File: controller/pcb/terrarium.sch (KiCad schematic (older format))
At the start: 53 parts, among them K1 G3MB-202P, K2 G3MB-202P, K3 G3MB-202P, Q1 S8050, Q2 S8050, Q3 S8050, SW1 RST, U1 ESP32-WROOM-32, U2 DS3231M, U5 TCA9548APWR

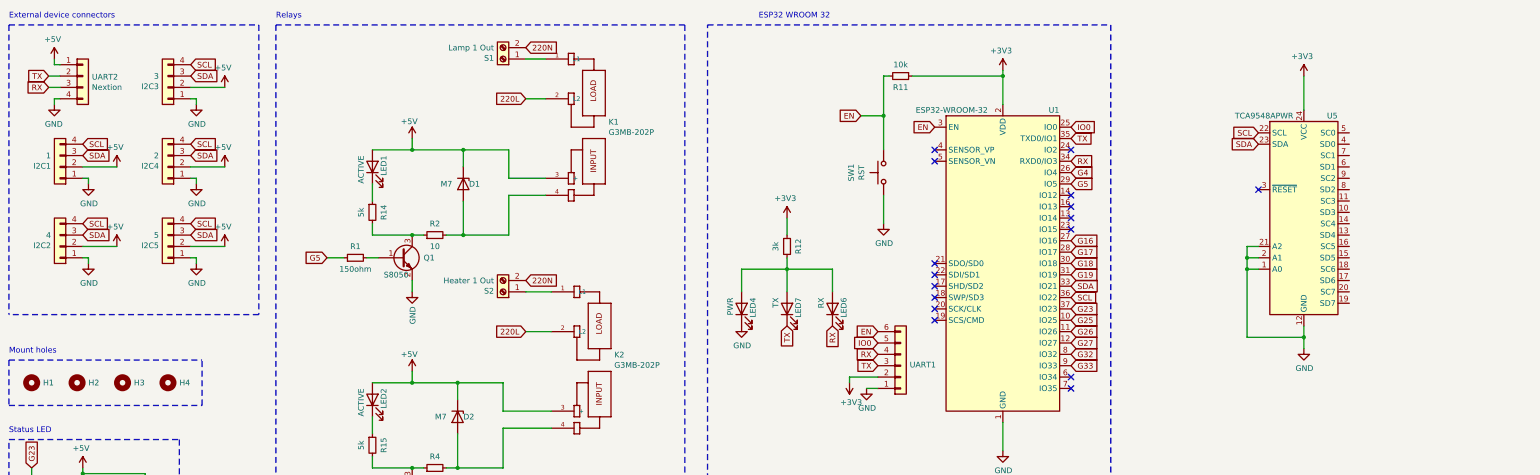
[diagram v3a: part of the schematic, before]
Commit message: add multiplexer for i2c, rearrange everything
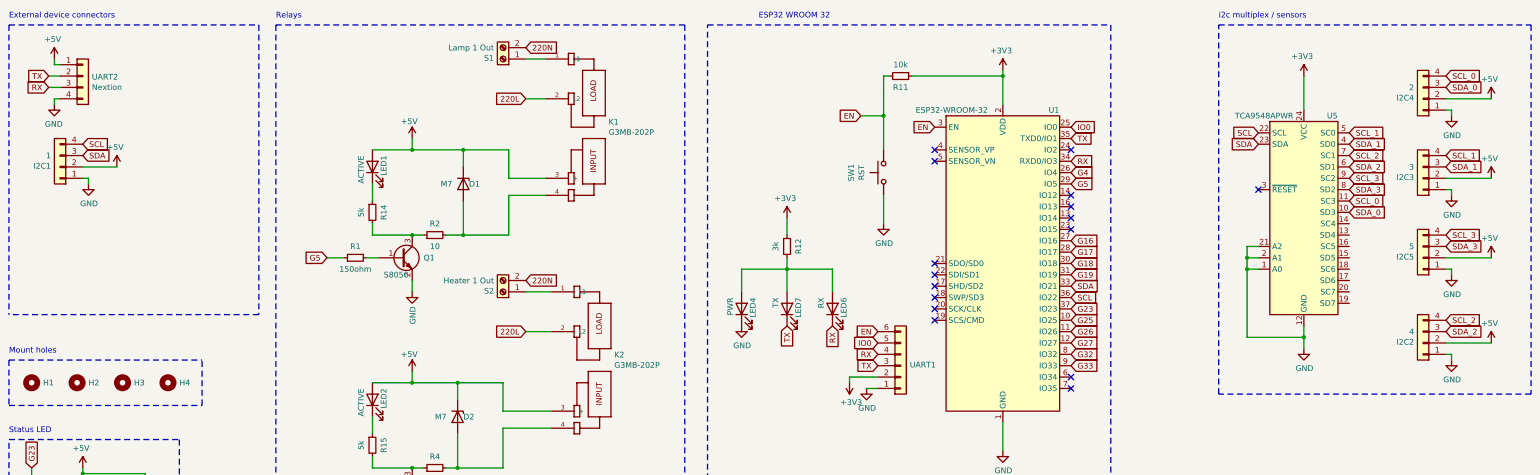
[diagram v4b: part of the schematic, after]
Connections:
- net SCL: no longer I2C2.4 (Pin_4), I2C3.4 (Pin_4), I2C4.4 (Pin_4), I2C5.4 (Pin_4)
- net SDA: no longer I2C2.3 (Pin_3), I2C3.3 (Pin_3), I2C4.3 (Pin_3), I2C5.3 (Pin_3)
- net SDA_0: now reaches U5.10 (SD3)
- net SDA_0: now also I2C4.3 (Pin_3)
- net SCL_0: now reaches U5.11 (SC3)
- net SCL_0: now also I2C4.4 (Pin_4)
- net SDA_1: now reaches U5.4 (SD0)
- net SDA_1: now also I2C3.3 (Pin_3)
- net SCL_1: now reaches U5.5 (SC0)
- net SCL_1: now also I2C3.4 (Pin_4)
- net SDA_2: now reaches U5.6 (SD1)
- net SDA_2: now also I2C2.3 (Pin_3)
- net SCL_2: now reaches U5.7 (SC1)
- net SCL_2: now also I2C2.4 (Pin_4)
- net SDA_3: now reaches U5.8 (SD2)
- net SDA_3: now also I2C5.3 (Pin_3)
- net SCL_3: now reaches U5.9 (SC2)
- net SCL_3: now also I2C5.4 (Pin_4)
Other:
- note added: "i2c multiplex / sensors"
- moved on the sheet: I2C2, I2C3, I2C4, I2C5
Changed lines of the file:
@@
 	1650 1950 1350 1950
-$Comp
-L Connector_Generic:Conn_01x04 I2C4
-U 1 1 6230B23A
-P 2100 1950
-F 0 "I2C4" H 2180 1942 50  0000 L CNN
-F 1 "2" H 2180 1851 50  0000 L CNN
-F 2 "Connector_JST:JST_XH_B4B-XH-AM_1x04_P2.50mm_Vertical" H 2100 1950 50  0001 C CNN
-F 3 "~" H 2100 1950 50  0001 C CNN
-	1    2100 1950
-	-1   0    0    1
-$EndComp
-Text GLabel 2300 1750 2    50   Input ~ 0
-SCL
-Text GLabel 2300 1850 2    50   Input ~ 0
-SDA
-$Comp
-L power:GND #PWR018
-U 1 1 6230B242
-P 2350 2100
-F 0 "#PWR018" H 2350 1850 50  0001 C CNN
-F 1 "GND" H 2355 1927 50  0000 C CNN
-F 2 "" H 2350 2100 50  0001 C CNN
-F 3 "" H 2350 2100 50  0001 C CNN
-	1    2350 2100
-	1    0    0    -1
-$EndComp
-Wire Wire Line
-	2350 2100 2350 2050
-Wire Wire Line
-	2350 2050 2300 2050
-$Comp
-L power:+5V #PWR021
-U 1 1 6230B24A
-P 2600 1950
-F 0 "#PWR021" H 2600 1800 50  0001 C CNN
-F 1 "+5V" H 2615 2123 50  0000 C CNN
-F 2 "" H 2600 1950 50  0001 C CNN
-F 3 "" H 2600 1950 50  0001 C CNN
-	1    2600 1950
-	-1   0    0    -1
-$EndComp
-Wire Wire Line
-	2600 1950 2300 1950
 $Comp
 L Connector_Generic:Conn_01x04 I2C2
 U 1 1 6231B2F4
-P 1150 2650
-F 0 "I2C2" H 1230 2642 50  0000 L CNN
-F 1 "4" H 1230 2551 50  0000 L CNN
-F 2 "Connector_JST:JST_XH_B4B-XH-AM_1x04_P2.50mm_Vertical" H 1150 2650 50  0001 C CNN
-F 3 "~" H 1150 2650 50  0001 C CNN
-	1    1150 2650
+P 13150 3500
+F 0 "I2C2" H 13230 3492 50  0000 L CNN
+F 1 "4" H 13230 3401 50  0000 L CNN
+F 2 "Connector_JST:JST_XH_B4B-XH-AM_1x04_P2.50mm_Vertical" H 13150 3500 50  0001 C CNN
+F 3 "~" H 13150 3500 50  0001 C CNN
+	1    13150 3500
 	-1   0    0    1
 $EndComp
-Text GLabel 1350 2450 2    50   Input ~ 0
-SCL
-Text GLabel 1350 2550 2    50   Input ~ 0
-SDA
+Text GLabel 13350 3300 2    50   Input ~ 0
+SCL_2
+Text GLabel 13350 3400 2    50   Input ~ 0
+SDA_2
 $Comp
 L power:GND #PWR014
 U 1 1 6231B2FC
-P 1400 2800
-F 0 "#PWR014" H 1400 2550 50  0001 C CNN
-F 1 "GND" H 1405 2627 50  0000 C CNN
-F 2 "" H 1400 2800 50  0001 C CNN
-F 3 "" H 1400 2800 50  0001 C CNN
-	1    1400 2800
-	1    0    0    -1
-$EndComp
-Wire Wire Line
-	1400 2800 1400 2750
-Wire Wire Line
-	1400 2750 1350 2750
+P 13400 3650
+F 0 "#PWR014" H 13400 3400 50  0001 C CNN
+F 1 "GND" H 13405 3477 50  0000 C CNN
+F 2 "" H 13400 3650 50  0001 C CNN
+F 3 "" H 13400 3650 50  0001 C CNN
+	1    13400 3650
+	1    0    0    -1
+$EndComp
+Wire Wire Line
+	13400 3650 13400 3600
+Wire Wire Line
+	13400 3600 13350 3600
 $Comp
 L power:+5V #PWR016
 U 1 1 6231B304
-P 1650 2650
-F 0 "#PWR016" H 1650 2500 50  0001 C CNN
-F 1 "+5V" H 1665 2823 50  0000 C CNN
-F 2 "" H 1650 2650 50  0001 C CNN
-F 3 "" H 1650 2650 50  0001 C CNN
-	1    1650 2650
-	-1   0    0    -1
-$EndComp
-Wire Wire Line
-	1650 2650 1350 2650
+P 13750 3500
+F 0 "#PWR016" H 13750 3350 50  0001 C CNN
+F 1 "+5V" H 13765 3673 50  0000 C CNN
+F 2 "" H 13750 3500 50  0001 C CNN
+F 3 "" H 13750 3500 50  0001 C CNN
+	1    13750 3500
+	-1   0    0    -1
+$EndComp
 $Comp
 L Connector_Generic:Conn_01x04 I2C5
 U 1 1 6232A2C4
-P 2100 2650
-F 0 "I2C5" H 2180 2642 50  0000 L CNN
-F 1 "5" H 2180 2551 50  0000 L CNN
-F 2 "Connector_JST:JST_XH_B4B-XH-AM_1x04_P2.50mm_Vertical" H 2100 2650 50  0001 C CNN
-F 3 "~" H 2100 2650 50  0001 C CNN
-	1    2100 2650
+P 13150 2750
+F 0 "I2C5" H 13230 2742 50  0000 L CNN
+F 1 "5" H 13230 2651 50  0000 L CNN
+F 2 "Connector_JST:JST_XH_B4B-XH-AM_1x04_P2.50mm_Vertical" H 13150 2750 50  0001 C CNN
+F 3 "~" H 13150 2750 50  0001 C CNN
+	1    13150 2750
 	-1   0    0    1
 $EndComp
-Text GLabel 2300 2450 2    50   Input ~ 0
-SCL
-Text GLabel 2300 2550 2    50   Input ~ 0
-SDA
+Text GLabel 13350 2550 2    50   Input ~ 0
+SCL_3
+Text GLabel 13350 2650 2    50   Input ~ 0
+SDA_3
 $Comp
 L power:GND #PWR019
 U 1 1 6232A2CC
-P 2350 2800
-F 0 "#PWR019" H 2350 2550 50  0001 C CNN
-F 1 "GND" H 2355 2627 50  0000 C CNN
-F 2 "" H 2350 2800 50  0001 C CNN
-F 3 "" H 2350 2800 50  0001 C CNN
-	1    2350 2800
-	1    0    0    -1
-$EndComp
-Wire Wire Line
-	2350 2800 2350 2750
-Wire Wire Line
-	2350 2750 2300 2750
+P 13400 2900
+F 0 "#PWR019" H 13400 2650 50  0001 C CNN
+F 1 "GND" H 13405 2727 50  0000 C CNN
+F 2 "" H 13400 2900 50  0001 C CNN
+F 3 "" H 13400 2900 50  0001 C CNN
+	1    13400 2900
+	1    0    0    -1
+$EndComp
+Wire Wire Line
+	13400 2900 13400 2850
+Wire Wire Line
+	13400 2850 13350 2850
 $Comp
 L power:+5V #PWR022
 U 1 1 6232A2D4
-P 2600 2650
-F 0 "#PWR022" H 2600 2500 50  0001 C CNN
-F 1 "+5V" H 2615 2823 50  0000 C CNN
-F 2 "" H 2600 2650 50  0001 C CNN
-F 3 "" H 2600 2650 50  0001 C CNN
-	1    2600 2650
-	-1   0    0    -1
-$EndComp
-Wire Wire Line
-	2600 2650 2300 2650
+P 13750 2750
+F 0 "#PWR022" H 13750 2600 50  0001 C CNN
+F 1 "+5V" H 13765 2923 50  0000 C CNN
+F 2 "" H 13750 2750 50  0001 C CNN
+F 3 "" H 13750 2750 50  0001 C CNN
+	1    13750 2750
+	-1   0    0    -1
+$EndComp
 $Comp
 L Connector_Generic:Conn_01x04 I2C3
 U 1 1 6233CBD6
-P 2100 1250
-F 0 "I2C3" H 2180 1242 50  0000 L CNN
-F 1 "3" H 2180 1151 50  0000 L CNN
-F 2 "Connector_JST:JST_XH_B4B-XH-AM_1x04_P2.50mm_Vertical" H 2100 1250 50  0001 C CNN
-F 3 "~" H 2100 1250 50  0001 C CNN
-	1    2100 1250
+P 13150 2050
+F 0 "I2C3" H 13230 2042 50  0000 L CNN
+F 1 "3" H 13230 1951 50  0000 L CNN
+F 2 "Connector_JST:JST_XH_B4B-XH-AM_1x04_P2.50mm_Vertical" H 13150 2050 50  0001 C CNN
+F 3 "~" H 13150 2050 50  0001 C CNN
+	1    13150 2050
 	-1   0    0    1
 $EndComp
-Text GLabel 2300 1050 2    50   Input ~ 0
-SCL
-Text GLabel 2300 1150 2    50   Input ~ 0
-SDA
+Text GLabel 13350 1850 2    50   Input ~ 0
+SCL_1
+Text GLabel 13350 1950 2    50   Input ~ 0
+SDA_1
 $Comp
 L power:GND #PWR017
 U 1 1 6233CBDE
-P 2350 1400
-F 0 "#PWR017" H 2350 1150 50  0001 C CNN
-F 1 "GND" H 2355 1227 50  0000 C CNN
-F 2 "" H 2350 1400 50  0001 C CNN
-F 3 "" H 2350 1400 50  0001 C CNN
-	1    2350 1400
-	1    0    0    -1
-$EndComp
-Wire Wire Line
-	2350 1400 2350 1350
-Wire Wire Line
-	2350 1350 2300 1350
+P 13400 2200
+F 0 "#PWR017" H 13400 1950 50  0001 C CNN
+F 1 "GND" H 13405 2027 50  0000 C CNN
+F 2 "" H 13400 2200 50  0001 C CNN
+F 3 "" H 13400 2200 50  0001 C CNN
+	1    13400 2200
+	1    0    0    -1
+$EndComp
+Wire Wire Line
+	13400 2200 13400 2150
+Wire Wire Line
+	13400 2150 13350 2150
 $Comp
 L power:+5V #PWR020
 U 1 1 6233CBE6
-P 2600 1250
-F 0 "#PWR020" H 2600 1100 50  0001 C CNN
-F 1 "+5V" H 2615 1423 50  0000 C CNN
-F 2 "" H 2600 1250 50  0001 C CNN
-F 3 "" H 2600 1250 50  0001 C CNN
-	1    2600 1250
-	-1   0    0    -1
-$EndComp
-Wire Wire Line
-	2600 1250 2300 1250
+P 13750 2050
+F 0 "#PWR020" H 13750 1900 50  0001 C CNN
+F 1 "+5V" H 13765 2223 50  0000 C CNN
+F 2 "" H 13750 2050 50  0001 C CNN
+F 3 "" H 13750 2050 50  0001 C CNN
+	1    13750 2050
+	-1   0    0    -1
+$EndComp
 Wire Notes Line
 	2900 3250 700  3250
@@
 Wire Wire Line
 	12100 1150 12100 1450
+Text GLabel 12500 2250 2    50   Input ~ 0
+SCL_0
+Text GLabel 12500 2350 2    50   Input ~ 0
+SDA_0
+Text GLabel 12500 1950 2    50   Input ~ 0
+SDA_2
+Text GLabel 12500 2150 2    50   Input ~ 0
+SDA_3
+Text GLabel 12500 2050 2    50   Input ~ 0
+SCL_3
+Text GLabel 12500 1650 2    50   Input ~ 0
+SCL_1
+Text GLabel 12500 1750 2    50   Input ~ 0
+SDA_1
+Text GLabel 12500 1850 2    50   Input ~ 0
+SCL_2
+$Comp
+L power:+5V #PWR021
+U 1 1 6230B24A
+P 13750 1350
+F 0 "#PWR021" H 13750 1200 50  0001 C CNN
+F 1 "+5V" H 13765 1523 50  0000 C CNN
+F 2 "" H 13750 1350 50  0001 C CNN
+F 3 "" H 13750 1350 50  0001 C CNN
+	1    13750 1350
+	-1   0    0    -1
+$EndComp
+Wire Wire Line
+	13400 1450 13350 1450
+Wire Wire Line
+	13400 1500 13400 1450
+$Comp
+L power:GND #PWR018
+U 1 1 6230B242
+P 13400 1500
+F 0 "#PWR018" H 13400 1250 50  0001 C CNN
+F 1 "GND" H 13405 1327 50  0000 C CNN
+F 2 "" H 13400 1500 50  0001 C CNN
+F 3 "" H 13400 1500 50  0001 C CNN
+	1    13400 1500
+	1    0    0    -1
+$EndComp
+Text GLabel 13350 1250 2    50   Input ~ 0
+SDA_0
+Text GLabel 13350 1150 2    50   Input ~ 0
+SCL_0
+$Comp
+L Connector_Generic:Conn_01x04 I2C4
+U 1 1 6230B23A
+P 13150 1350
+F 0 "I2C4" H 13230 1342 50  0000 L CNN
+F 1 "2" H 13230 1251 50  0000 L CNN
+F 2 "Connector_JST:JST_XH_B4B-XH-AM_1x04_P2.50mm_Vertical" H 13150 1350 50  0001 C CNN
+F 3 "~" H 13150 1350 50  0001 C CNN
+	1    13150 1350
+	-1   0    0    1
+$EndComp
+Wire Wire Line
+	13350 1350 13750 1350
+Wire Wire Line
+	13350 2050 13750 2050
+Wire Wire Line
+	13350 3500 13750 3500
+Wire Wire Line
+	13350 2750 13750 2750
+Wire Notes Line
+	11350 700  14100 700
+Wire Notes Line
+	14100 700  14100 3950
+Wire Notes Line
+	14100 3950 11350 3950
+Wire Notes Line
+	11350 3950 11350 700
+Text Notes 11350 650  0    50   ~ 0
+i2c multiplex / sensors
 $EndSCHEMATC
